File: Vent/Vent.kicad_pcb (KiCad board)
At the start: 2 copper layers, 2 parts, among them J1 Conn_01x03, U1 ESP32-C3-WROOM-02-N4

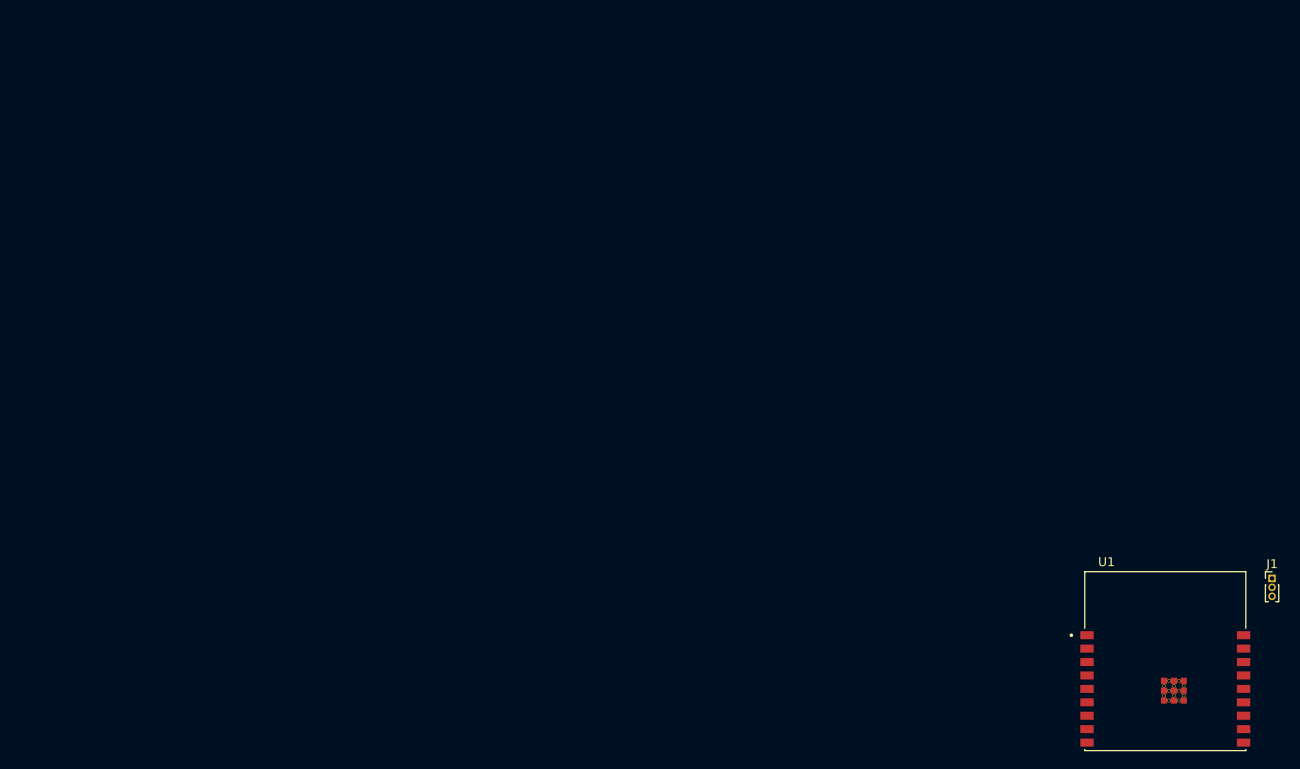
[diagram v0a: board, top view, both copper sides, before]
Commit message: electronics: Sync latest designs from working directory
- Rename Puck board files (was Vent.kicad_* → Puck.kicad_*)
- Add full Comps libraries (footprints, models, symbols) for all four boards
- Add manufacturing-current/ Gerber outputs and renders for all boards
- Add new components: ESP32-C6-MINI-1 (Puck), ESP32-H2-MINI-1 (Vent), NCU15XH103F60RC (BMS)
- Add PCM JLCPCB passive symbol libraries across all boards
- Add per-project .gitignore files and Autoprogramming/AUTOPROGRAMMING_REVIEW.md
- Add root-level BOM files, sourcing audit, and manufacturing readiness ledger
- Update KiCad design files and Gerbers for BMS, Autoprogramming, and Vent

Co-Authored-By: Claude Sonnet 4.6 <noreply@anthropic.com>

Original-author: Zachariah K. Sharma <zachariah.sharma@gmail.com>
Source-commit: 261c676a3a26a8c60302274465dd756769088335
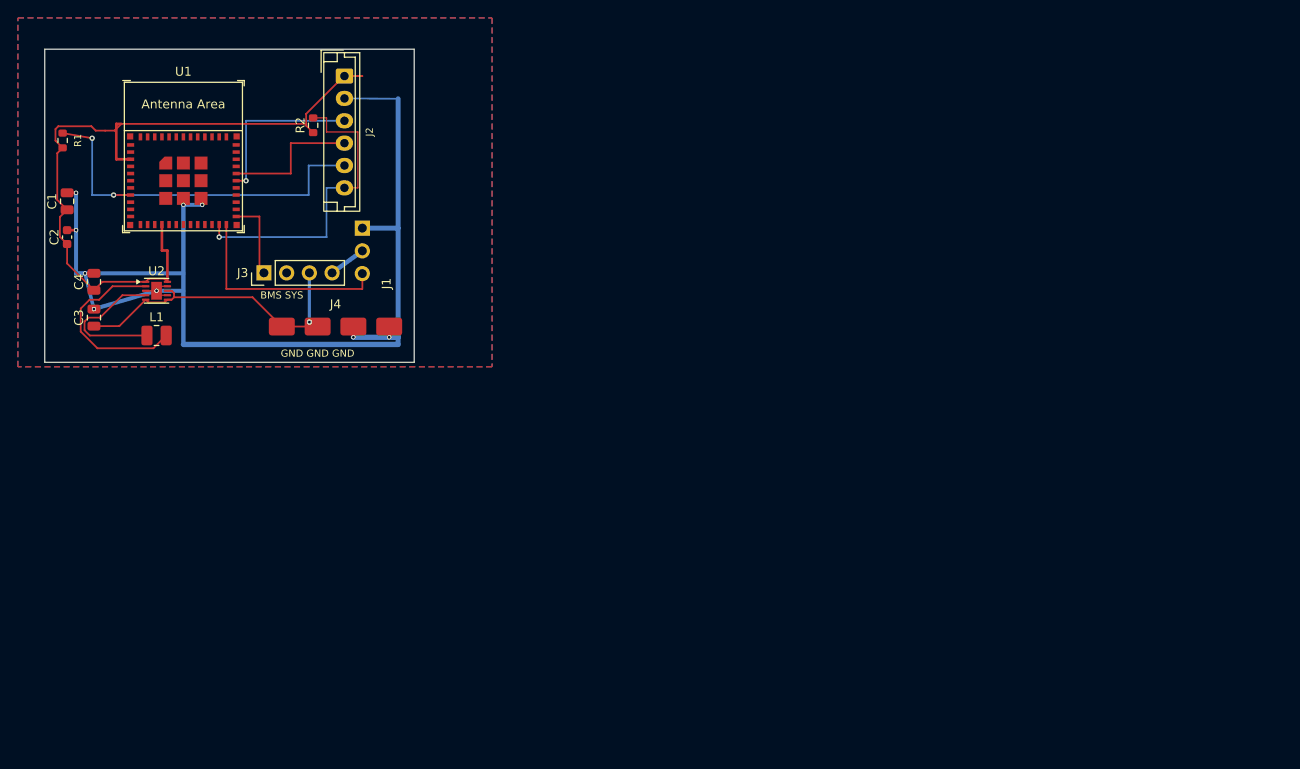
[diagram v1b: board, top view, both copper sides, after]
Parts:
- added C1: 10uF, Capacitor_SMD:C_0805_2012Metric, F.Cu at (14.0, 29.0)
- added C2: 100nF, Capacitor_SMD:C_0603_1608Metric, F.Cu at (14.0, 33.0)
- added C3: 10uF VIN, Capacitor_SMD:C_0805_2012Metric, F.Cu at (17.0, 42.0)
- added C4: 22uF VOUT, Capacitor_SMD:C_0805_2012Metric, F.Cu at (17.0, 38.0)
- added J2: AUTO_PROG_HDR, Connector_JST:JST_EH_B6B-EH-A_1x06_P2.50mm_Vertical, F.Cu at (45.0, 15.0)
- added J3: SERVO_5V_BOOST_MODULE, Footprints:PinHeader_1x04_P2.54mm_Vertical, F.Cu at (36.0, 37.0)
- added J4: BMS_SPRING_CONTACTS, VentPads:BMS_SpringLeafContacts_1x04_P4mm, F.Cu at (38.0, 43.0)
- added L1: 2.2uH, Inductor_SMD:L_1008_2520Metric, F.Cu at (24.0, 44.0)
- added R1: 10k EN pullup, Resistor_SMD:R_0603_1608Metric, F.Cu at (13.5, 22.2)
- added R2: 10k BOOT pullup, Resistor_SMD:R_0603_1608Metric, F.Cu at (41.5, 20.5)
- added U2: TPS63031DSK, Package_SON:WSON-10-1EP_2.5x2.5mm_P0.5mm_EP1.2x2mm, F.Cu at (24.0, 39.0)
- J1: value Conn_01x03 -> SG90_SERVO; footprint Connector_PinHeader_1.00mm:PinHeader_1x03_P1.00mm_Vertical -> Footprints:PinHeader_1x03_P2.54mm_Vertical
- U1: value ESP32-C3-WROOM-02-N4 -> ESP32-H2-MINI-1-H4S; footprint Footprints:MODULE_ESP32-C3-WROOM-02-H4 -> Footprints:ESP32-H2-MINI-1
- moved U1 123.4 mm to (27.0, 24.0)
- moved J1 109.0 mm to (47.0, 32.0)
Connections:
- J1 pad 1: unconnected-(J1-Pin_1-Pad1) -> GND
- J1 pad 2: unconnected-(J1-Pin_2-Pad2) -> +5V_SERVO
- J1 pad 3: unconnected-(J1-Pin_3-Pad3) -> SERVO_PWM
- U1 pad 1: +3V3 -> GND
- U1 pad 10: unconnected-(U1-IO10-Pad10) -> (no net)
- U1 pad 11: unconnected-(U1-RXD-Pad11) -> GND
- U1 pad 12: unconnected-(U1-TXD-Pad12) -> (no net)
- U1 pad 13: unconnected-(U1-IO18-Pad13) -> (no net)
- U1 pad 14: unconnected-(U1-IO19-Pad14) -> GND
- U1 pad 15: unconnected-(U1-IO3-Pad15) -> +3V3
- U1 pad 16: unconnected-(U1-IO2-Pad16) -> (no net)
- U1 pad 17: unconnected-(U1-IO1-Pad17) -> (no net)
- U1 pad 18: unconnected-(U1-IO0-Pad18) -> (no net)
- U1 pad 19: GND -> (no net)
- U1 pad 2: unconnected-(U1-EN-Pad2) -> GND
- U1 pad 20: GND -> (no net)
- U1 pad 21: GND -> (no net)
- U1 pad 22: GND -> (no net)
- U1 pad 23: GND -> ESP_BOOT
- U1 pad 24: GND -> SERVO_PWM
- U1 pad 25: GND -> SERVO_BOOST_EN
- U1 pad 26: GND -> (no net)
- U1 pad 27: GND -> (no net)
- U1 pad 28: GND -> (no net)
- U1 pad 29: GND -> (no net)
- U1 pad 3: unconnected-(U1-IO4-Pad3) -> +3V3
- U1 pad 30: GND -> ESP_RXD
- U1 pad 31: GND -> ESP_TXD
- U1 pad 32: GND -> (no net)
- U1 pad 33: GND -> (no net)
- U1 pad 34: GND -> (no net)
- U1 pad 35: GND -> (no net)
- U1 pad 4: unconnected-(U1-IO5-Pad4) -> (no net)
- U1 pad 5: unconnected-(U1-IO6-Pad5) -> (no net)
- U1 pad 6: unconnected-(U1-IO7-Pad6) -> (no net)
- U1 pad 7: unconnected-(U1-IO8-Pad7) -> (no net)
- U1 pad 8: unconnected-(U1-IO9-Pad8) -> ESP_EN
- U1 pad 9: GND -> (no net)
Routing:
- net GND: track 0.00 -> 132.6 mm, vias 0 -> 9
- net +3V3: track 0.00 -> 84.1 mm
- net ESP_EN: track 0.00 -> 43.1 mm, vias 0 -> 2
- net BMS_SYS_CONTACT: track 0.00 -> 35.8 mm, vias 0 -> 1
- net ESP_BOOT: track 0.00 -> 35.2 mm, vias 0 -> 1
- net SERVO_PWM: track 0.00 -> 24.1 mm
- net BB_SW2: track 0.00 -> 21.8 mm
- net ESP_RXD: track 0.00 -> 18.8 mm, vias 0 -> 1
- net BB_SW1: track 0.00 -> 16.2 mm
- net ESP_TXD: track 0.00 -> 15.5 mm
- net SERVO_BOOST_EN: track 0.00 -> 9.40 mm
- net +5V_SERVO: track 0.00 -> 4.18 mm
- added copper zone on B.Cu, net GND
- added copper zone on F.Cu, net GND
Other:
- board outline added: 41.3 x 35 mm
- board text added: "BMS SYS"
- board text added: "GND GND GND"
